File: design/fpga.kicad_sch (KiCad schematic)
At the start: 80 parts, among them J7 DEBUG_FPGA_GPIO, J8 DIGILENT_JTAG_HS2_01X06, SW1 RST, SW2 PROG, U13 XC7S15-FTGB196, U14 IS25LP064A-JKx

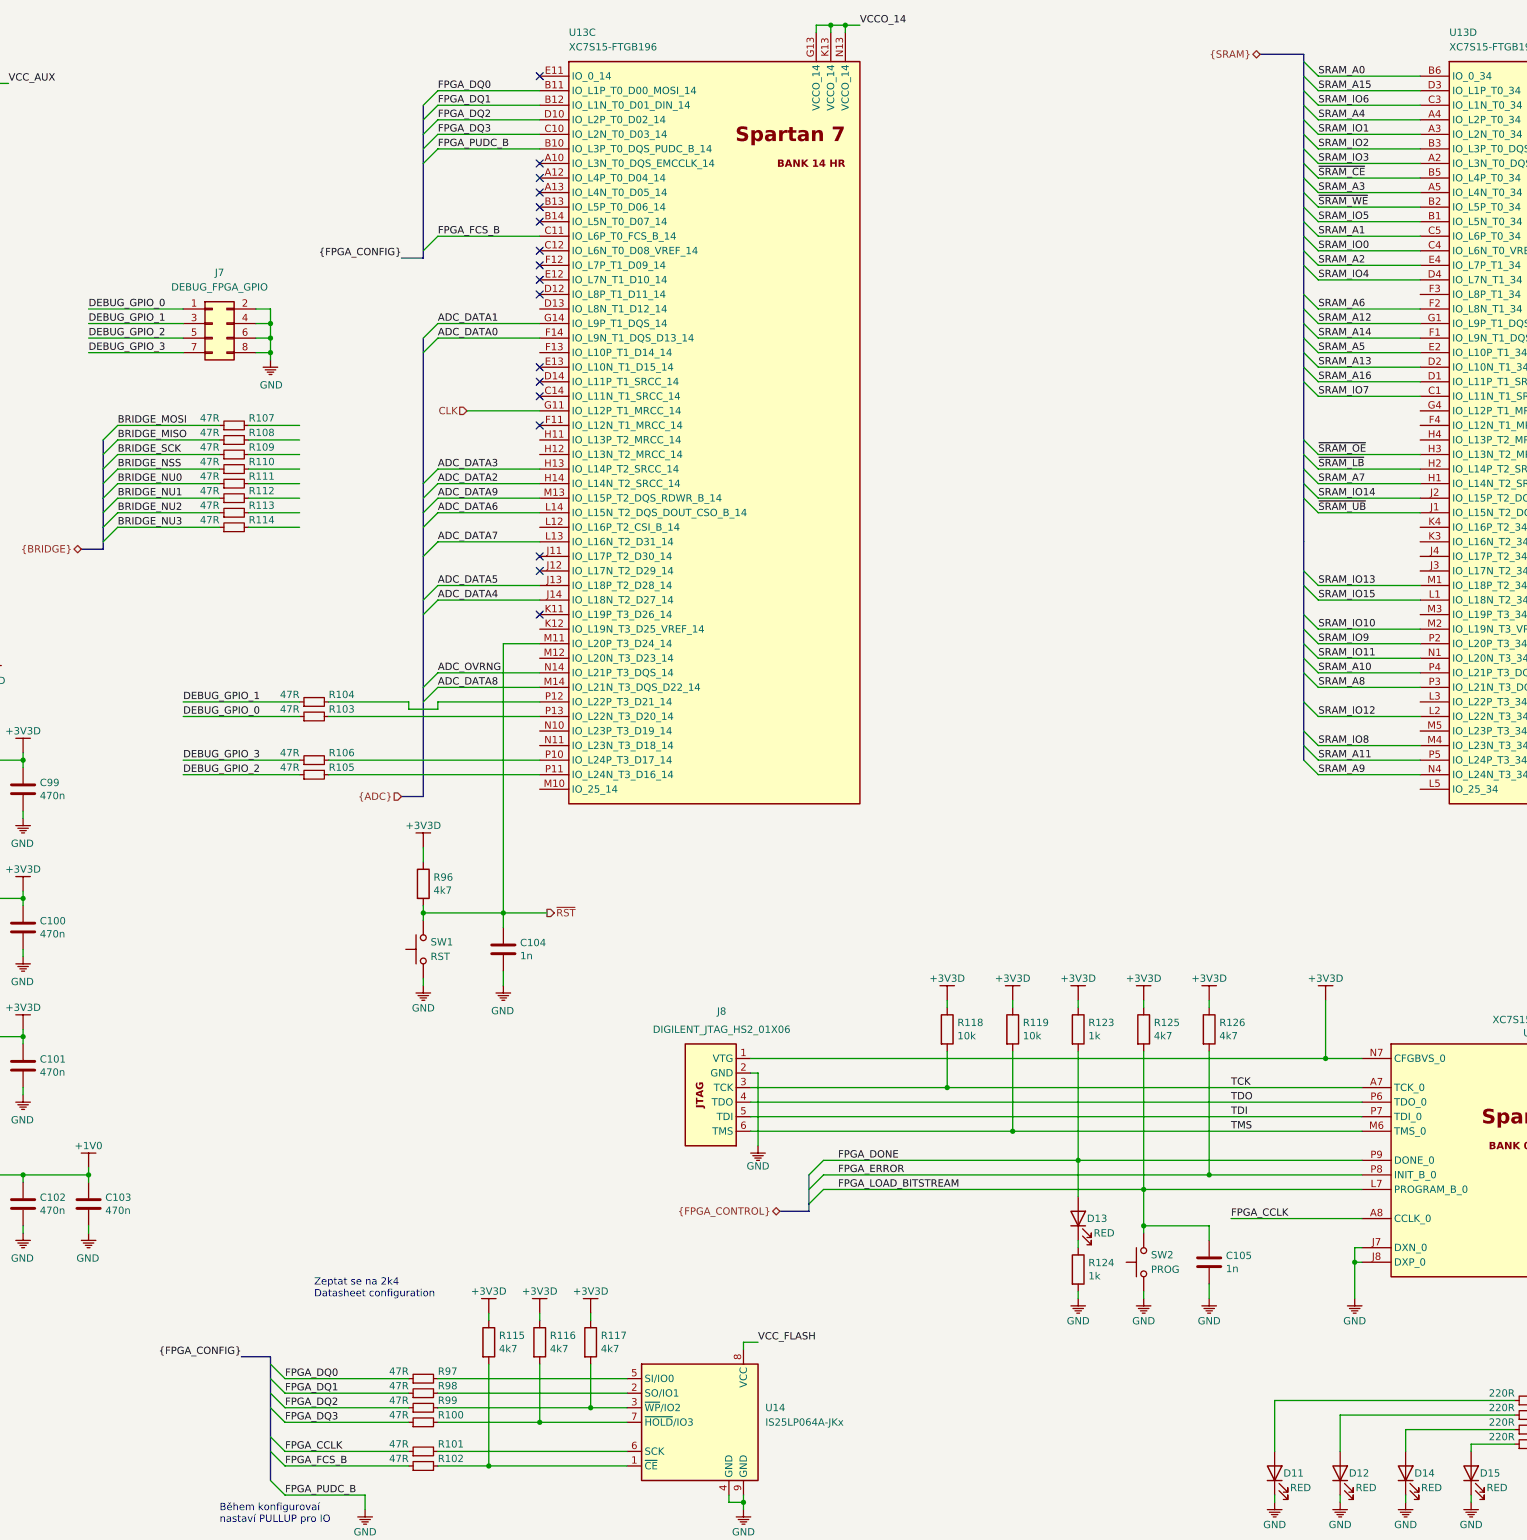
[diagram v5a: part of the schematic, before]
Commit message: Created new RAM placement and test layout
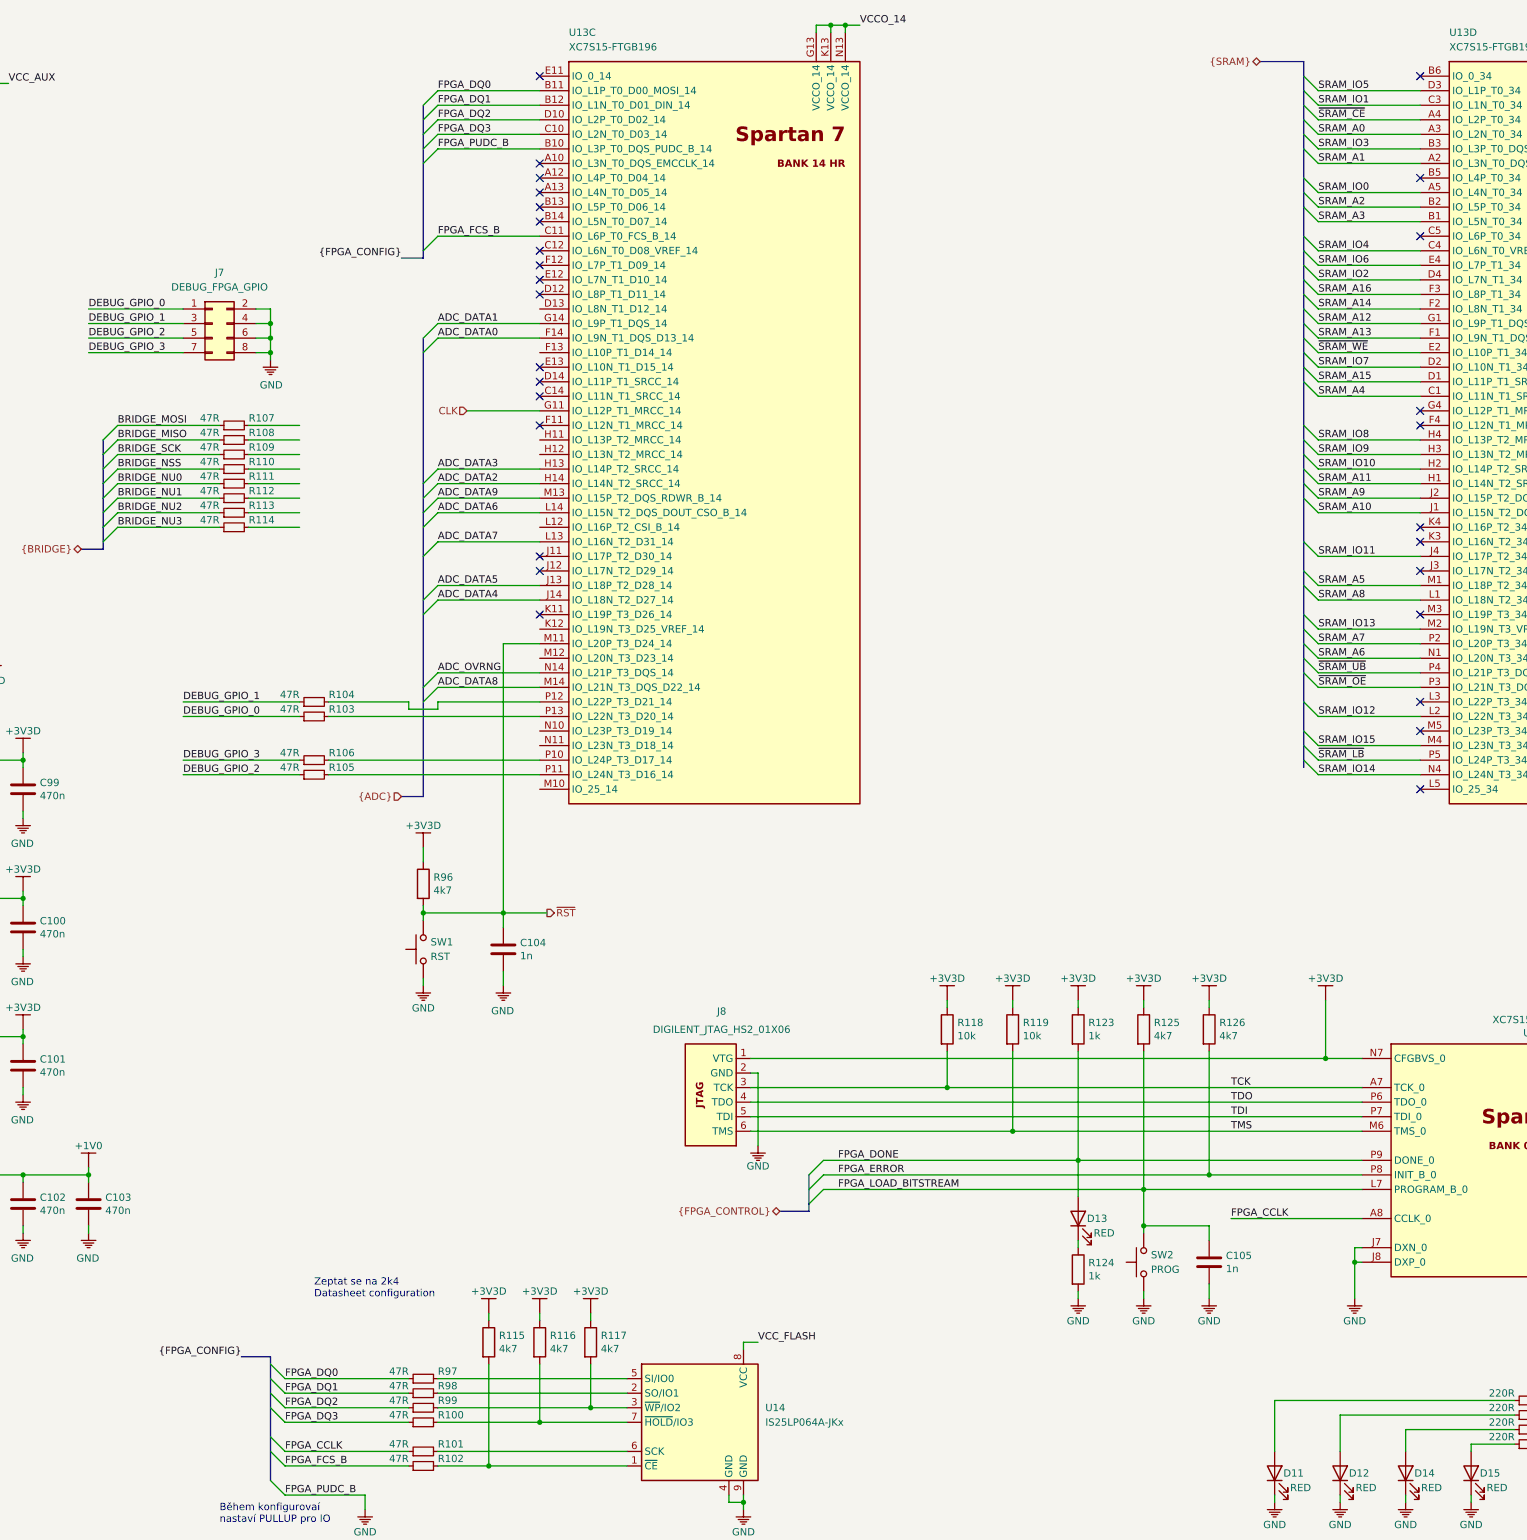
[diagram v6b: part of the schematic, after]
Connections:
- net SRAM_A0: now also U13.A3 (IO_L2N_T0_34); no longer U13.B6 (IO_0_34)
- net SRAM_A1: now also U13.A2 (IO_L3N_T0_DQS_34); no longer U13.C5 (IO_L6P_T0_34)
- net SRAM_A10: now also U13.J1 (IO_L15N_T2_DQS_34); no longer U13.P4 (IO_L21P_T3_DQS_34)
- net SRAM_A11: now also U13.H1 (IO_L14N_T2_SRCC_34); no longer U13.P5 (IO_L24P_T3_34)
- net SRAM_A13: now also U13.F1 (IO_L9N_T1_DQS_34); no longer U13.D2 (IO_L10N_T1_34)
- net SRAM_A14: now also U13.F2 (IO_L8N_T1_34); no longer U13.F1 (IO_L9N_T1_DQS_34)
- net SRAM_A15: now also U13.D1 (IO_L11P_T1_SRCC_34); no longer U13.D3 (IO_L1P_T0_34)
- net SRAM_A16: now also U13.F3 (IO_L8P_T1_34); no longer U13.D1 (IO_L11P_T1_SRCC_34)
- net SRAM_A2: now also U13.B2 (IO_L5P_T0_34); no longer U13.E4 (IO_L7P_T1_34)
- net SRAM_A3: now also U13.B1 (IO_L5N_T0_34); no longer U13.A5 (IO_L4N_T0_34)
- net SRAM_A4: now also U13.C1 (IO_L11N_T1_SRCC_34); no longer U13.A4 (IO_L2P_T0_34)
- net SRAM_A5: now also U13.M1 (IO_L18P_T2_34); no longer U13.E2 (IO_L10P_T1_34)
- net SRAM_A6: now also U13.N1 (IO_L20N_T3_34); no longer U13.F2 (IO_L8N_T1_34)
- net SRAM_A7: now also U13.P2 (IO_L20P_T3_34); no longer U13.H1 (IO_L14N_T2_SRCC_34)
- net SRAM_A8: now also U13.L1 (IO_L18N_T2_34); no longer U13.P3 (IO_L21N_T3_DQS_34)
- net SRAM_A9: now also U13.J2 (IO_L15P_T2_DQS_34); no longer U13.N4 (IO_L24N_T3_34)
- net SRAM_IO0: now also U13.A5 (IO_L4N_T0_34); no longer U13.C4 (IO_L6N_T0_VREF_34)
- net SRAM_IO1: now also U13.C3 (IO_L1N_T0_34); no longer U13.A3 (IO_L2N_T0_34)
- net SRAM_IO10: now also U13.H2 (IO_L14P_T2_SRCC_34); no longer U13.M2 (IO_L19N_T3_VREF_34)
- net SRAM_IO11: now also U13.J4 (IO_L17P_T2_34); no longer U13.N1 (IO_L20N_T3_34)
- net SRAM_IO13: now also U13.M2 (IO_L19N_T3_VREF_34); no longer U13.M1 (IO_L18P_T2_34)
- net SRAM_IO14: now also U13.N4 (IO_L24N_T3_34); no longer U13.J2 (IO_L15P_T2_DQS_34)
- net SRAM_IO15: now also U13.M4 (IO_L23N_T3_34); no longer U13.L1 (IO_L18N_T2_34)
- net SRAM_IO2: now also U13.D4 (IO_L7N_T1_34); no longer U13.B3 (IO_L3P_T0_DQS_34)
- net SRAM_IO3: now also U13.B3 (IO_L3P_T0_DQS_34); no longer U13.A2 (IO_L3N_T0_DQS_34)
- net SRAM_IO4: now also U13.C4 (IO_L6N_T0_VREF_34); no longer U13.D4 (IO_L7N_T1_34)
- net SRAM_IO5: now also U13.D3 (IO_L1P_T0_34); no longer U13.B1 (IO_L5N_T0_34)
- net SRAM_IO6: now also U13.E4 (IO_L7P_T1_34); no longer U13.C3 (IO_L1N_T0_34)
- net SRAM_IO7: now also U13.D2 (IO_L10N_T1_34); no longer U13.C1 (IO_L11N_T1_SRCC_34)
- net SRAM_IO8: now also U13.H4 (IO_L13P_T2_MRCC_34); no longer U13.M4 (IO_L23N_T3_34)
- net SRAM_IO9: now also U13.H3 (IO_L13N_T2_MRCC_34); no longer U13.P2 (IO_L20P_T3_34)
- net ~SRAM_CE: now also U13.A4 (IO_L2P_T0_34); no longer U13.B5 (IO_L4P_T0_34)
- net ~SRAM_LB: now also U13.P5 (IO_L24P_T3_34); no longer U13.H2 (IO_L14P_T2_SRCC_34)
- net ~SRAM_OE: now also U13.P3 (IO_L21N_T3_DQS_34); no longer U13.H3 (IO_L13N_T2_MRCC_34)
- net ~SRAM_UB: now also U13.P4 (IO_L21P_T3_DQS_34); no longer U13.J1 (IO_L15N_T2_DQS_34)
- net ~SRAM_WE: now also U13.E2 (IO_L10P_T1_34); no longer U13.B2 (IO_L5P_T0_34)
- no-connect marks 17 -> 29

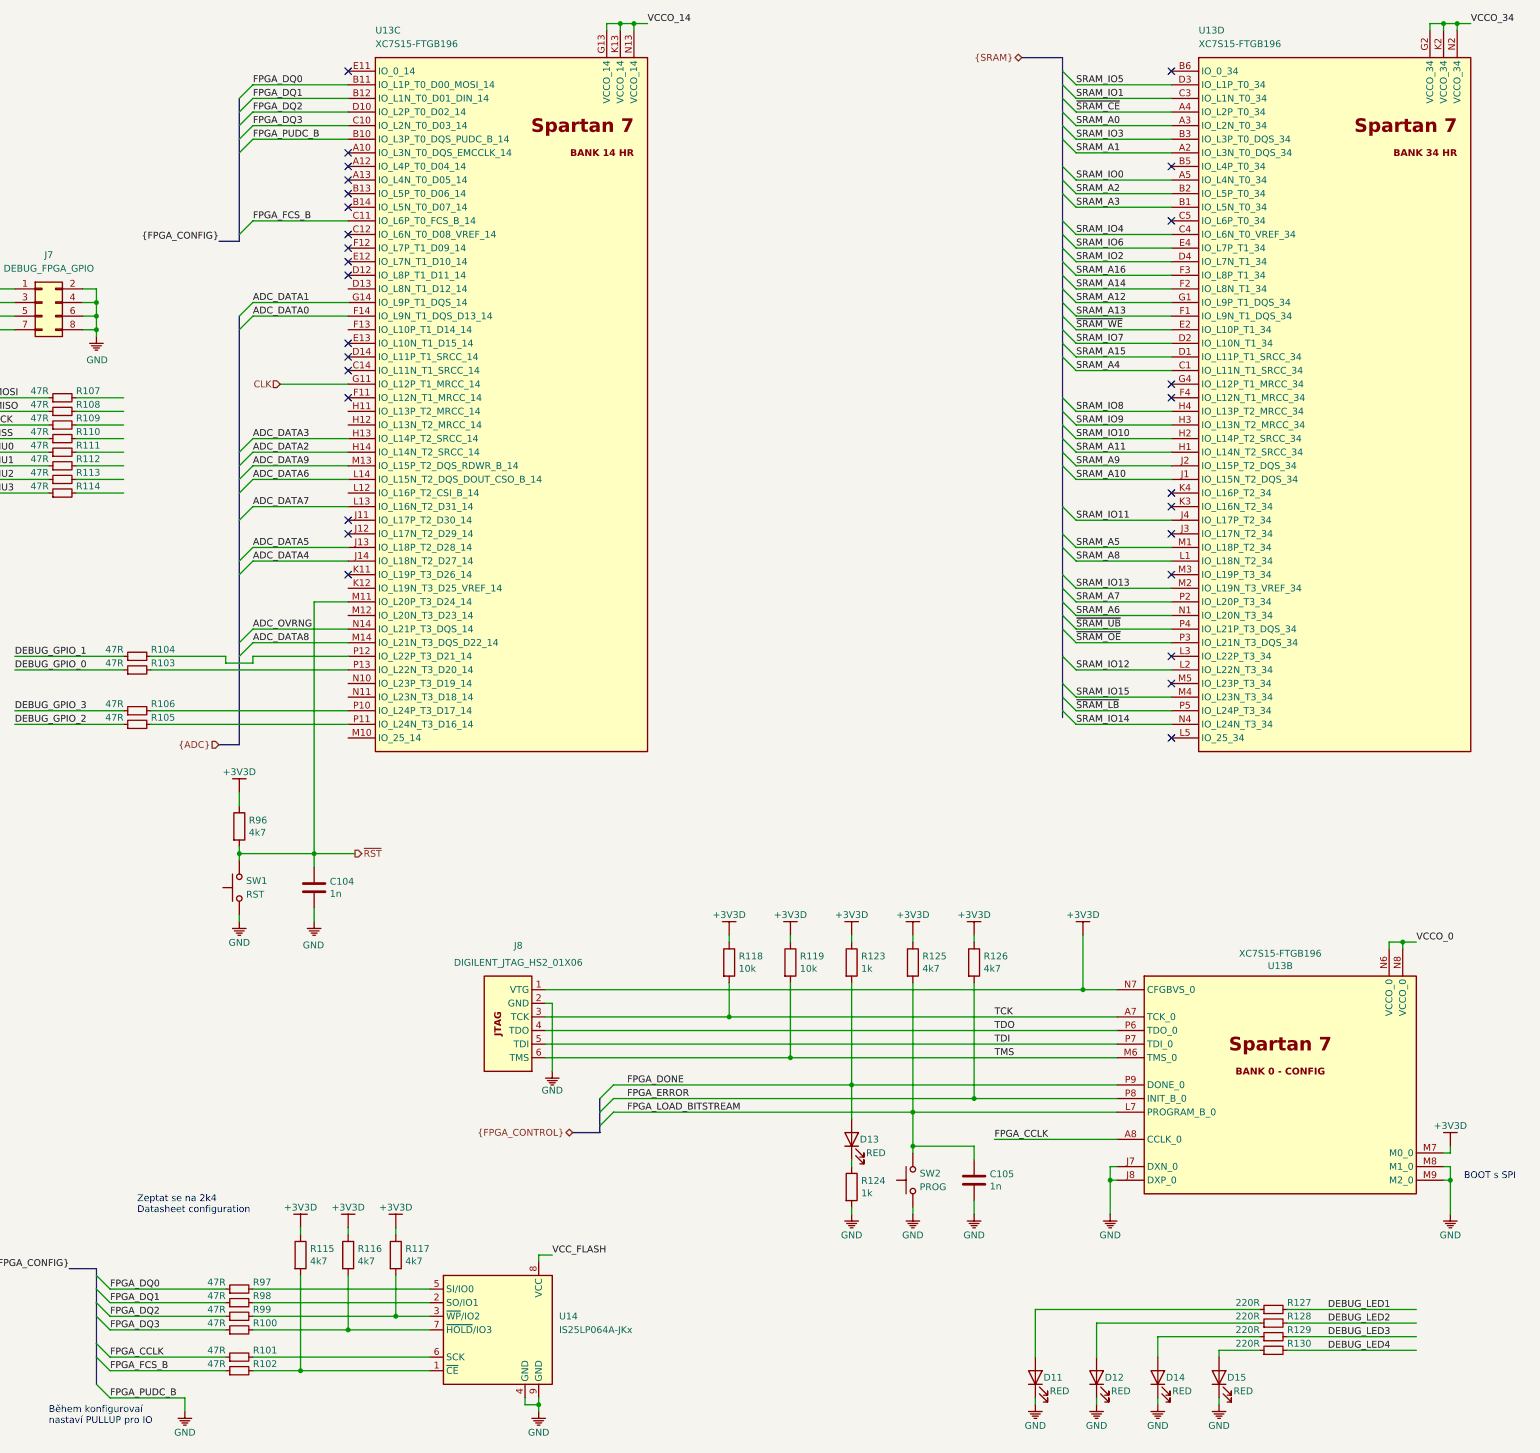
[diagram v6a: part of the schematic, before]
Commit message: Added FPGA LEDs layout
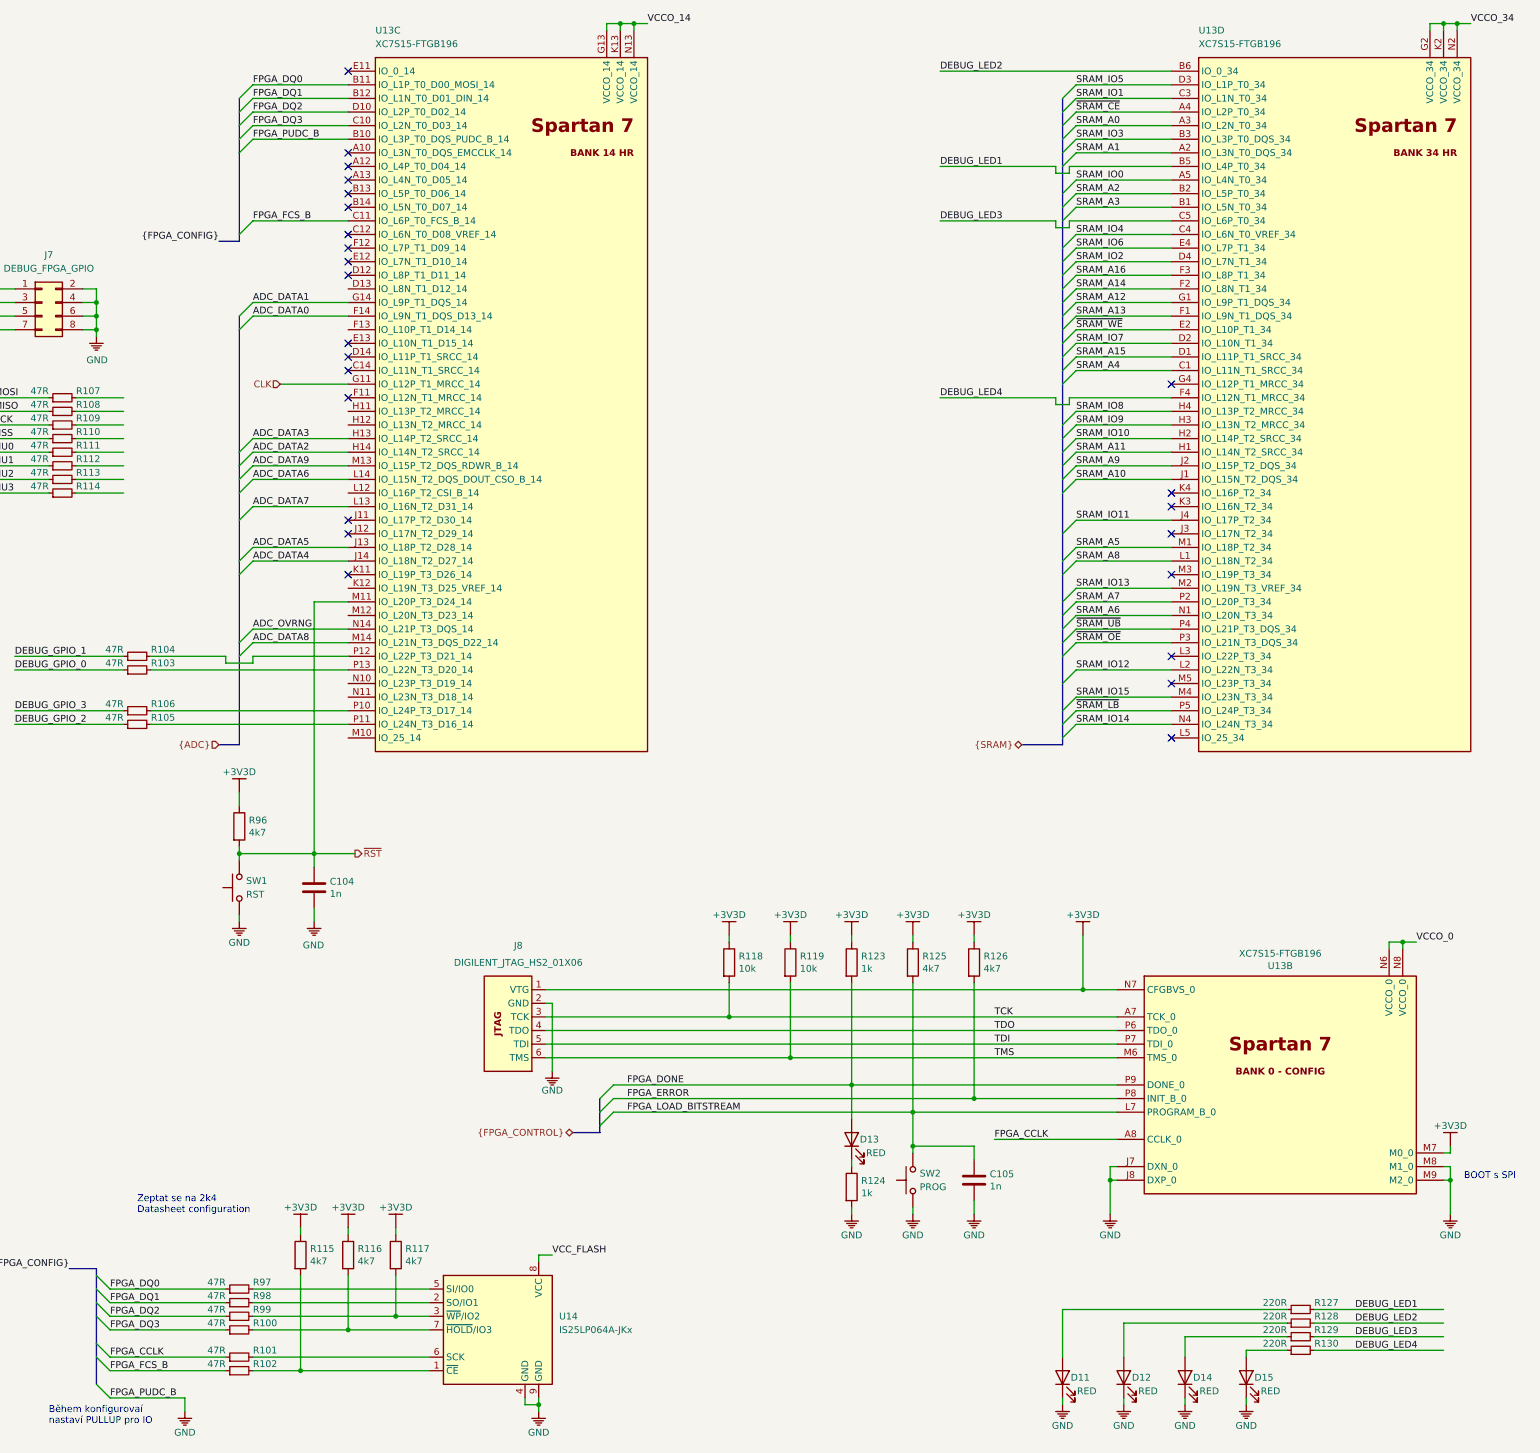
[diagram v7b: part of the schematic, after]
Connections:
- net DEBUG_LED1: now also U13.B5 (IO_L4P_T0_34)
- net DEBUG_LED2: now also U13.B6 (IO_0_34)
- net DEBUG_LED3: now also U13.C5 (IO_L6P_T0_34)
- net DEBUG_LED4: now also U13.F4 (IO_L12N_T1_MRCC_34)
- no-connect marks 29 -> 25
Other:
- moved on the sheet: D11, D12, D14, D15, R127, R128, R129, R130
